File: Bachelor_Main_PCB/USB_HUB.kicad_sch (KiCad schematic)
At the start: 15 parts, among them J11 M20-9990245, U6 USB2514B-I/M2

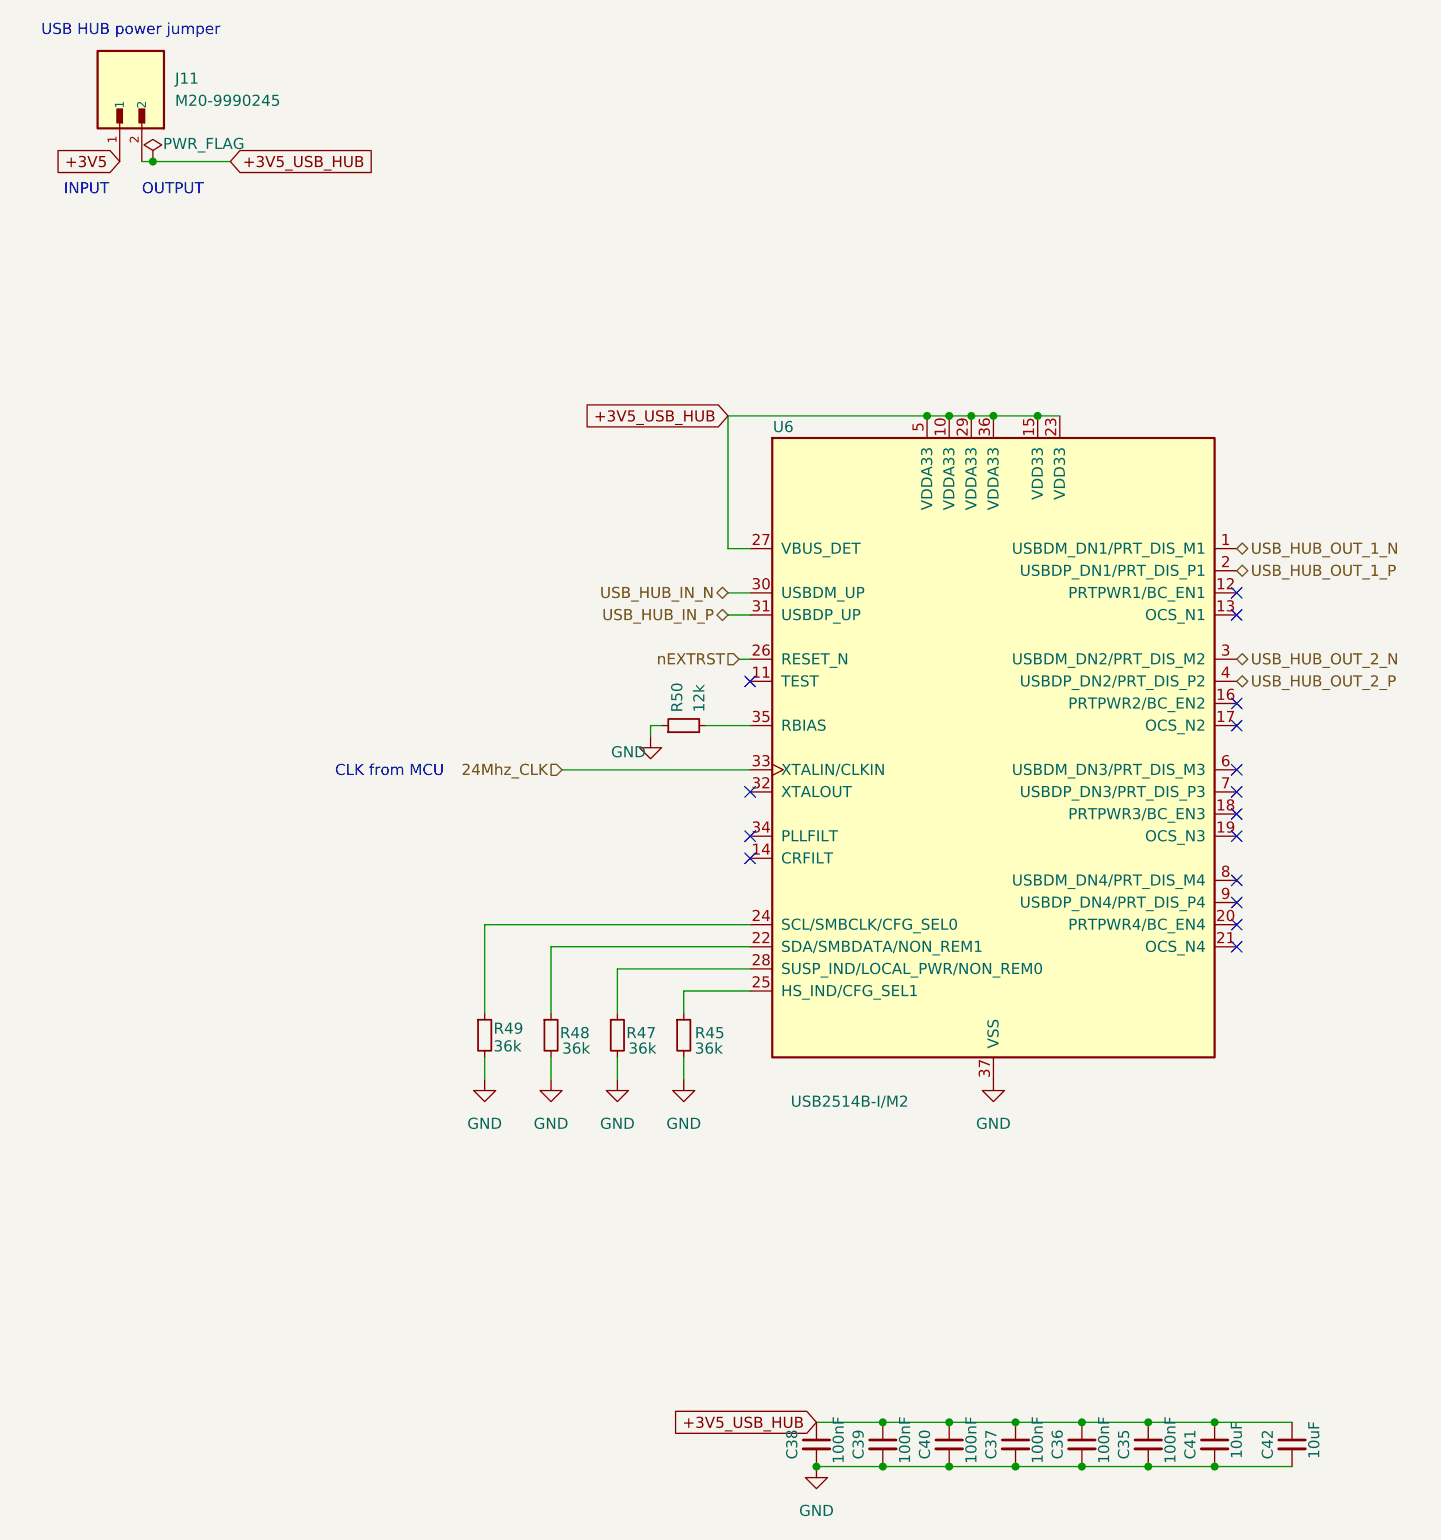
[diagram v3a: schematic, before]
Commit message: Imported components from schematic to PCB and Reanotat all designators
THis means every designator is now different and the references made prior no longer applies
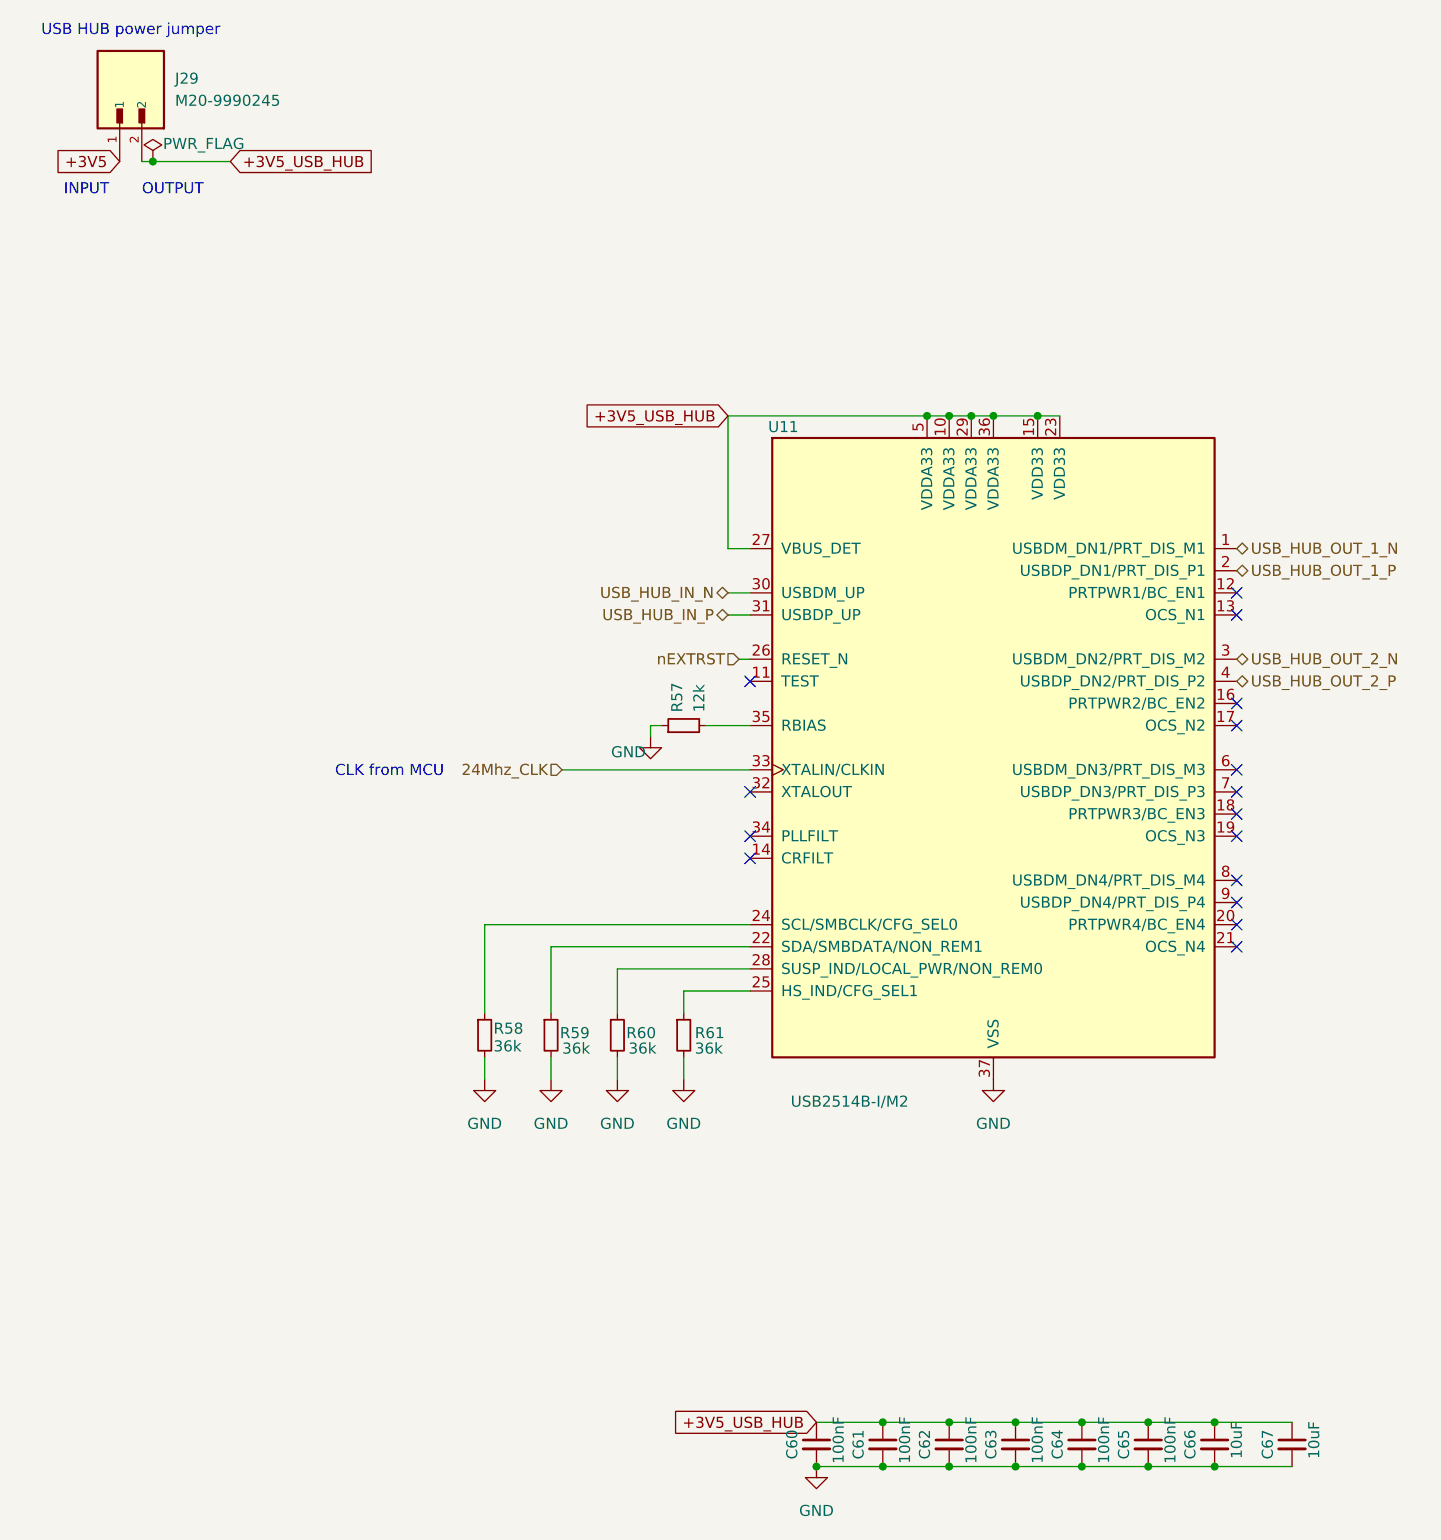
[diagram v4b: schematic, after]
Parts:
- renumbered C38 to C60, C39 to C61, C40 to C62, C37 to C63, C36 to C64, C35 to C65, C41 to C66, C42 to C67, J11 to J29, R50 to R57, R49 to R58, R48 to R59, R47 to R60, R45 to R61, U6 to U11
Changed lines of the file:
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@@
 		(on_board yes)
 		(dnp no)
-		(property "Reference" "U6"
+		(property "Reference" "U11"
 			(at 106.68 63.5 0)
 			(effects
@@
 			(project "Bachelor_Main_PCB"
 				(path "/3544d663-329e-4884-b753-28436ca187e8/a2efe210-cbe4-4166-b2f4-897451b29d8a"
-					(reference "U6")
+					(reference "U11")
 					(unit 1)
 				)
@@
 		(on_board yes)
 		(dnp no)
-		(property "Reference" "C40"
+		(property "Reference" "C62"
 			(at 122.936 180.34 90)
 			(effects
@@
 			(project "Bachelor_Main_PCB"
 				(path "/3544d663-329e-4884-b753-28436ca187e8/a2efe210-cbe4-4166-b2f4-897451b29d8a"
-					(reference "C40")
+					(reference "C62")
 					(unit 1)
 				)
@@
 		(dnp no)
 		(fields_autoplaced yes)
-		(property "Reference" "#PWR029"
+		(property "Reference" "#PWR0101"
 			(at 72.39 144.78 0)
 			(effects
@@
 			(project ""
 				(path "/3544d663-329e-4884-b753-28436ca187e8/a2efe210-cbe4-4166-b2f4-897451b29d8a"
-					(reference "#PWR029")
+					(reference "#PWR0101")
 					(unit 1)
 				)
@@
 		(dnp no)
 		(fields_autoplaced yes)
-		(property "Reference" "#PWR026"
+		(property "Reference" "#PWR0104"
 			(at 95.25 144.78 0)
 			(effects
@@
 			(project ""
 				(path "/3544d663-329e-4884-b753-28436ca187e8/a2efe210-cbe4-4166-b2f4-897451b29d8a"
-					(reference "#PWR026")
+					(reference "#PWR0104")
 					(unit 1)
 				)
@@
 		(on_board yes)
 		(dnp no)
-		(property "Reference" "C41"
+		(property "Reference" "C66"
 			(at 153.416 180.34 90)
 			(effects
@@
 			(project "Bachelor_Main_PCB"
 				(path "/3544d663-329e-4884-b753-28436ca187e8/a2efe210-cbe4-4166-b2f4-897451b29d8a"
-					(reference "C41")
+					(reference "C66")
 					(unit 1)
 				)
@@
 		(on_board yes)
 		(dnp no)
-		(property "Reference" "R49"
+		(property "Reference" "R58"
 			(at 73.406 132.588 0)
 			(effects
@@
 			(project "Bachelor_Main_PCB"
 				(path "/3544d663-329e-4884-b753-28436ca187e8/a2efe210-cbe4-4166-b2f4-897451b29d8a"
-					(reference "R49")
+					(reference "R58")
 					(unit 1)
 				)
@@
 		(on_board yes)
 		(dnp no)
-		(property "Reference" "C37"
+		(property "Reference" "C63"
 			(at 130.556 180.34 90)
 			(effects
@@
 			(project "Bachelor_Main_PCB"
 				(path "/3544d663-329e-4884-b753-28436ca187e8/a2efe210-cbe4-4166-b2f4-897451b29d8a"
-					(reference "C37")
+					(reference "C63")
 					(unit 1)
 				)
@@
 		(on_board yes)
 		(dnp no)
-		(property "Reference" "R50"
+		(property "Reference" "R57"
 			(at 94.488 96.266 0)
 			(effects
@@
 			(project "Bachelor_Main_PCB"
 				(path "/3544d663-329e-4884-b753-28436ca187e8/a2efe210-cbe4-4166-b2f4-897451b29d8a"
-					(reference "R50")
+					(reference "R57")
 					(unit 1)
 				)
@@
 		(dnp no)
 		(fields_autoplaced yes)
-		(property "Reference" "J11"
+		(property "Reference" "J29"
 			(at 36.83 23.4949 90)
 			(effects
@@
 			(project "Bachelor_Main_PCB"
 				(path "/3544d663-329e-4884-b753-28436ca187e8/a2efe210-cbe4-4166-b2f4-897451b29d8a"
-					(reference "J11")
+					(reference "J29")
 					(unit 1)
 				)
@@
 		(on_board yes)
 		(dnp no)
-		(property "Reference" "C35"
+		(property "Reference" "C65"
 			(at 145.796 180.34 90)
 			(effects
@@
 			(project "Bachelor_Main_PCB"
 				(path "/3544d663-329e-4884-b753-28436ca187e8/a2efe210-cbe4-4166-b2f4-897451b29d8a"
-					(reference "C35")
+					(reference "C65")
 					(unit 1)
 				)
@@
 		(on_board yes)
 		(dnp no)
-		(property "Reference" "#FLG05"
+		(property "Reference" "#FLG017"
 			(at 34.29 31.115 0)
 			(effects
@@
 			(project "Bachelor_Main_PCB"
 				(path "/3544d663-329e-4884-b753-28436ca187e8/a2efe210-cbe4-4166-b2f4-897451b29d8a"
-					(reference "#FLG05")
+					(reference "#FLG017")
 					(unit 1)
 				)
@@
 		(dnp no)
 		(fields_autoplaced yes)
-		(property "Reference" "#PWR028"
+		(property "Reference" "#PWR0102"
 			(at 80.01 144.78 0)
 			(effects
@@
 			(project ""
 				(path "/3544d663-329e-4884-b753-28436ca187e8/a2efe210-cbe4-4166-b2f4-897451b29d8a"
-					(reference "#PWR028")
+					(reference "#PWR0102")
 					(unit 1)
 				)
@@
 		(on_board yes)
 		(dnp no)
-		(property "Reference" "R48"
+		(property "Reference" "R59"
 			(at 81.026 133.096 0)
 			(effects
@@
 			(project "Bachelor_Main_PCB"
 				(path "/3544d663-329e-4884-b753-28436ca187e8/a2efe210-cbe4-4166-b2f4-897451b29d8a"
-					(reference "R48")
+					(reference "R59")
 					(unit 1)
 				)
@@
 		(on_board yes)
 		(dnp no)
-		(property "Reference" "C38"
+		(property "Reference" "C60"
 			(at 107.696 180.34 90)
 			(effects
@@
 			(project "Bachelor_Main_PCB"
 				(path "/3544d663-329e-4884-b753-28436ca187e8/a2efe210-cbe4-4166-b2f4-897451b29d8a"
-					(reference "C38")
+					(reference "C60")
 					(unit 1)
 				)
@@
 		(dnp no)
 		(fields_autoplaced yes)
-		(property "Reference" "#PWR027"
+		(property "Reference" "#PWR0103"
 			(at 87.63 144.78 0)
 			(effects
@@
 			(project ""
 				(path "/3544d663-329e-4884-b753-28436ca187e8/a2efe210-cbe4-4166-b2f4-897451b29d8a"
-					(reference "#PWR027")
+					(reference "#PWR0103")
 					(unit 1)
 				)
@@
 		(dnp no)
 		(fields_autoplaced yes)
-		(property "Reference" "#PWR033"
+		(property "Reference" "#PWR0106"
 			(at 110.49 189.23 0)
 			(effects
@@
 			(project "Bachelor_Main_PCB"
 				(path "/3544d663-329e-4884-b753-28436ca187e8/a2efe210-cbe4-4166-b2f4-897451b29d8a"
-					(reference "#PWR033")
+					(reference "#PWR0106")
 					(unit 1)
 				)
@@
 		(dnp no)
 		(fields_autoplaced yes)
-		(property "Reference" "#PWR030"
+		(property "Reference" "#PWR0105"
 			(at 130.81 144.78 0)
 			(effects
@@
 			(project "Bachelor_Main_PCB"
 				(path "/3544d663-329e-4884-b753-28436ca187e8/a2efe210-cbe4-4166-b2f4-897451b29d8a"
-					(reference "#PWR030")
+					(reference "#PWR0105")
 					(unit 1)
 				)
@@
 		(on_board yes)
 		(dnp no)
-		(property "Reference" "#PWR031"
+		(property "Reference" "#PWR0100"
 			(at 91.44 105.41 0)
 			(effects
@@
 			(project "Bachelor_Main_PCB"
 				(path "/3544d663-329e-4884-b753-28436ca187e8/a2efe210-cbe4-4166-b2f4-897451b29d8a"
-					(reference "#PWR031")
+					(reference "#PWR0100")
 					(unit 1)
 				)
@@
 		(on_board yes)
 		(dnp no)
-		(property "Reference" "R47"
+		(property "Reference" "R60"
 			(at 88.646 133.096 0)
 			(effects
@@
 			(project "Bachelor_Main_PCB"
 				(path "/3544d663-329e-4884-b753-28436ca187e8/a2efe210-cbe4-4166-b2f4-897451b29d8a"
-					(reference "R47")
+					(reference "R60")
 					(unit 1)
 				)
@@
 		(on_board yes)
 		(dnp no)
-		(property "Reference" "C39"
+		(property "Reference" "C61"
 			(at 115.316 180.34 90)
 			(effects
@@
 			(project "Bachelor_Main_PCB"
 				(path "/3544d663-329e-4884-b753-28436ca187e8/a2efe210-cbe4-4166-b2f4-897451b29d8a"
-					(reference "C39")
+					(reference "C61")
 					(unit 1)
 				)
@@
 		(on_board yes)
 		(dnp no)
-		(property "Reference" "C42"
+		(property "Reference" "C67"
 			(at 162.306 180.34 90)
 			(effects
@@
 			(project "Bachelor_Main_PCB"
 				(path "/3544d663-329e-4884-b753-28436ca187e8/a2efe210-cbe4-4166-b2f4-897451b29d8a"
-					(reference "C42")
+					(reference "C67")
 					(unit 1)
 				)
@@
 		(on_board yes)
 		(dnp no)
-		(property "Reference" "R45"
+		(property "Reference" "R61"
 			(at 96.52 133.096 0)
 			(effects
@@
 			(project "Bachelor_Main_PCB"
 				(path "/3544d663-329e-4884-b753-28436ca187e8/a2efe210-cbe4-4166-b2f4-897451b29d8a"
-					(reference "R45")
+					(reference "R61")
 					(unit 1)
 				)
@@
 		(on_board yes)
 		(dnp no)
-		(property "Reference" "C36"
+		(property "Reference" "C64"
 			(at 138.176 180.34 90)
 			(effects
@@
 			(project "Bachelor_Main_PCB"
 				(path "/3544d663-329e-4884-b753-28436ca187e8/a2efe210-cbe4-4166-b2f4-897451b29d8a"
-					(reference "C36")
+					(reference "C64")
 					(unit 1)
 				)

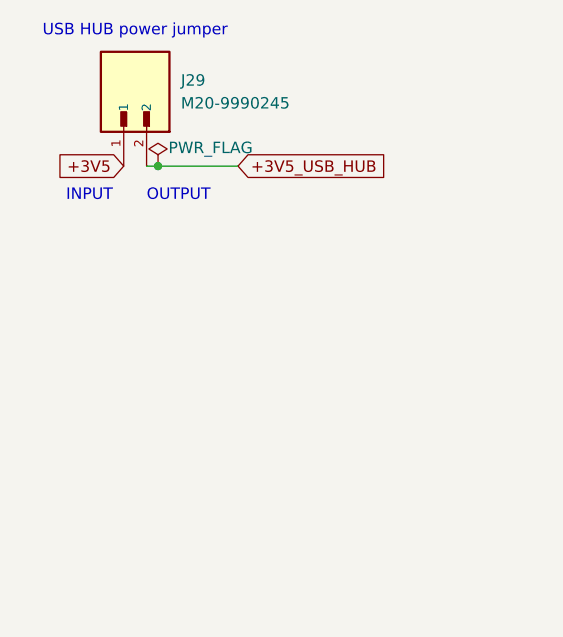
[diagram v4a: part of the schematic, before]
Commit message: Add LED to USB_HUB
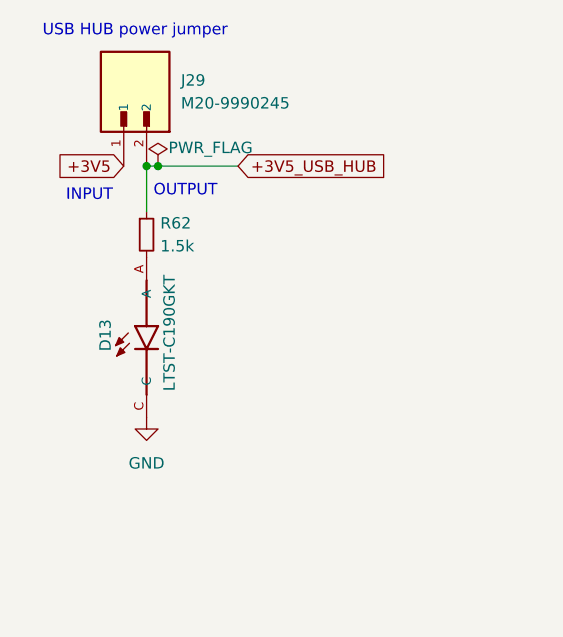
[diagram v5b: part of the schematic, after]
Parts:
- added D13: LTST-C190GKT, LTST-C190GKT:LEDM1608X80, symbol LTST-C190GKT:LTST-C190GKT
- added R62: 1.5k, Resistor_SMD:R_0603_1608Metric, symbol Device:R_Small
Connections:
- net +3V5_USB_HUB: now also R62.1
- net GND: now also D13.C
- new net: D13.A, R62.2
